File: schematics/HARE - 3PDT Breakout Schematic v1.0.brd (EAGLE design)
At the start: 30.5 x 20 mm, 4 parts, among them SW1 3PDTBLUE

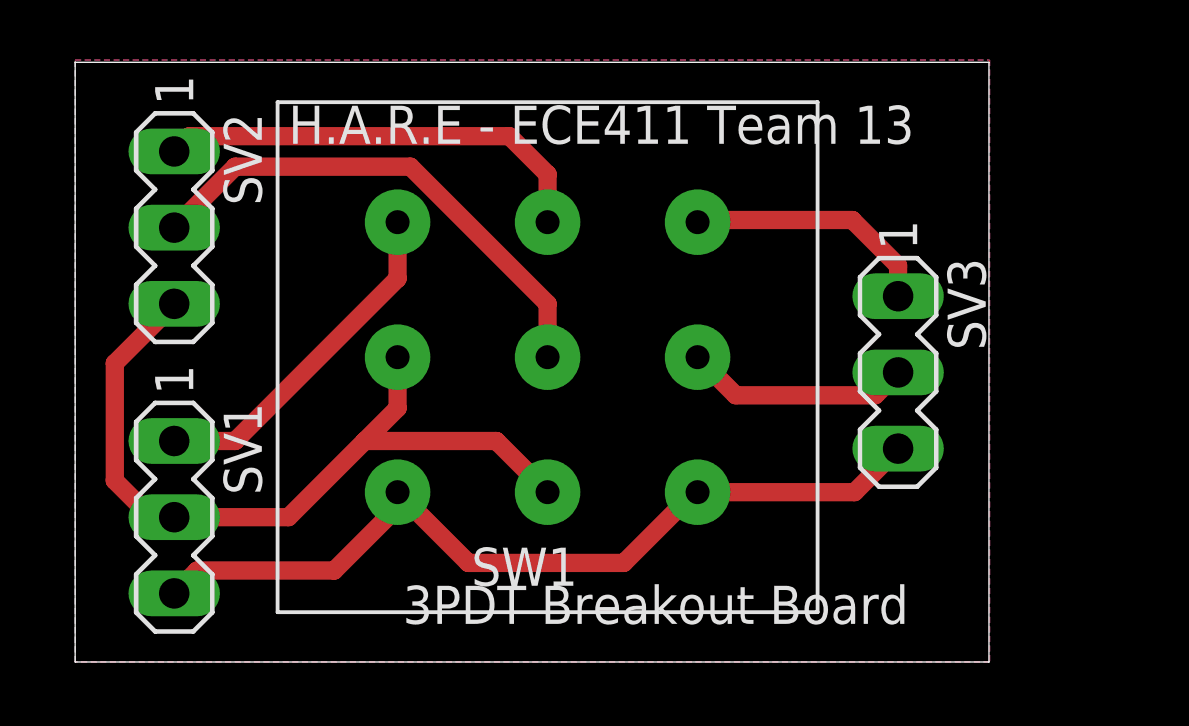
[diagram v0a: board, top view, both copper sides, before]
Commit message: adapting 3PDT breakout board to mate with HARE main board
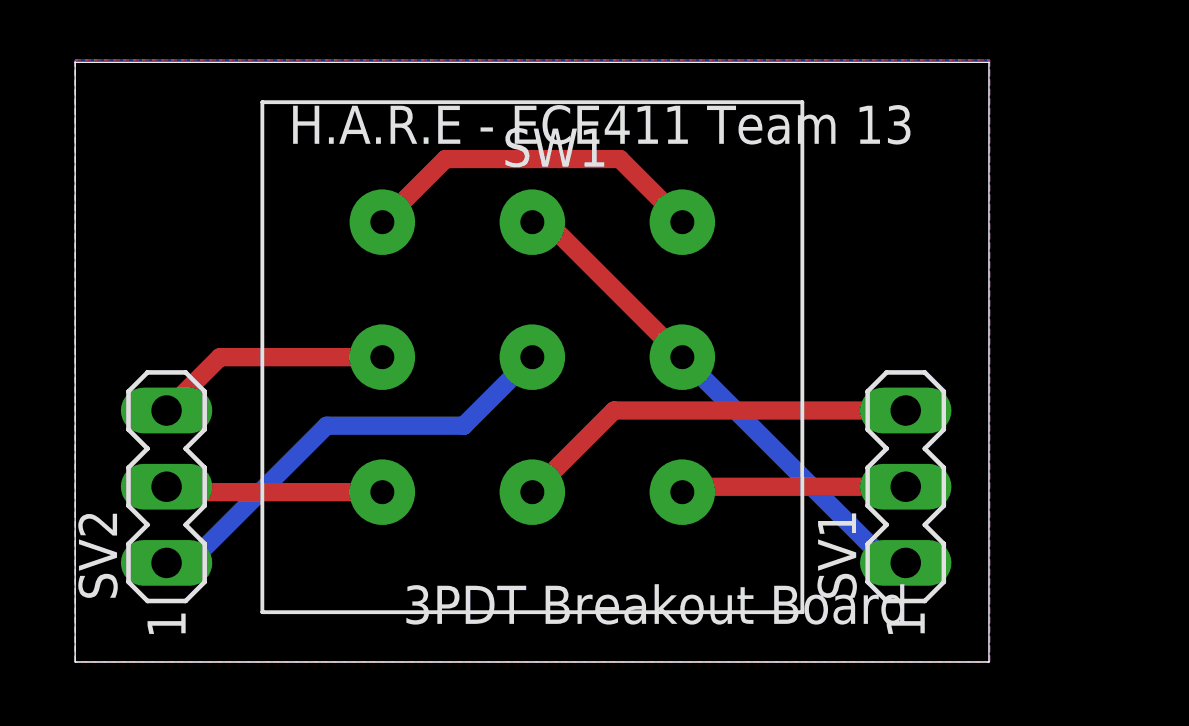
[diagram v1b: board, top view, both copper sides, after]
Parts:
- removed SV3: (no value), con-lstb:MA03-1
- moved SV1 24.4 mm to (27.7, 5.84), turned to 90 degrees
- moved SV2 8.64 mm to (3.05, 5.84), turned to 90 degrees
- moved SW1 0.51 mm to (15.2, 10.2), turned to 180 degrees
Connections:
- net ANALOG_IN: now also SV1.2; no longer SV1.1
- net ANALOG_OUT: now also SV2.3; no longer SV3.2
- net BYPASS: no longer SV1.3, SV3.3
- net GND: now also SV2.1; no longer SV2.2
- net INPUT: now also SV1.1; no longer SV1.2, SV2.3
- net OUTPUT: now also SV2.2; no longer SV3.1
- net PWR_LED: now also SV1.3; no longer SV2.1
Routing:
- net BYPASS: track 28.4 -> 11.8 mm
- net INPUT: track 26.7 -> 17.2 mm
- net ANALOG_IN: track 11.6 -> 7.52 mm
- net GND: track 17.0 -> 15.0 mm
- net PWR_LED: track 14.8 -> 13.6 mm
- net OUTPUT: track 8.36 -> 7.27 mm
- added copper zone on layer 16, net N$1
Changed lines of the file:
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@@
 <?xml version="1.0" encoding="utf-8"?>
 <!DOCTYPE eagle SYSTEM "eagle.dtd">
-<eagle version="8.4.0">
+<eagle version="8.4.1">
 <drawing>
 <settings>
@@
 <param name="dpMaxLengthDifference" value="10mm"/>
 <param name="dpGapFactor" value="2.5"/>
+<param name="checkAngle" value="0"/>
 <param name="checkFont" value="1"/>
 <param name="checkRestrict" value="1"/>
@@
 </autorouter>
 <elements>
-<element name="SW1" library="gm-switches" package="CHINABLUE" value="3PDTBLUE" x="15.748" y="10.16"/>
-<element name="SV1" library="con-lstb" package="MA03-1" value="" x="3.302" y="4.826" rot="R270">
-<attribute name="MF" value="" x="3.302" y="4.826" size="1.778" layer="27" rot="R270" display="off"/>
-<attribute name="MPN" value="" x="3.302" y="4.826" size="1.778" layer="27" rot="R270" display="off"/>
-<attribute name="OC_FARNELL" value="unknown" x="3.302" y="4.826" size="1.778" layer="27" rot="R270" display="off"/>
-<attribute name="OC_NEWARK" value="unknown" x="3.302" y="4.826" size="1.778" layer="27" rot="R270" display="off"/>
+<element name="SW1" library="gm-switches" package="CHINABLUE" value="3PDTBLUE" x="15.24" y="10.16" rot="R180"/>
+<element name="SV1" library="con-lstb" package="MA03-1" value="" x="27.686" y="5.842" rot="R90">
+<attribute name="MF" value="" x="27.686" y="5.842" size="1.778" layer="27" rot="R90" display="off"/>
+<attribute name="MPN" value="" x="27.686" y="5.842" size="1.778" layer="27" rot="R90" display="off"/>
+<attribute name="OC_FARNELL" value="unknown" x="27.686" y="5.842" size="1.778" layer="27" rot="R90" display="off"/>
+<attribute name="OC_NEWARK" value="unknown" x="27.686" y="5.842" size="1.778" layer="27" rot="R90" display="off"/>
 </element>
-<element name="SV2" library="con-lstb" package="MA03-1" value="" x="3.302" y="14.478" rot="R270">
-<attribute name="MF" value="" x="3.302" y="14.478" size="1.778" layer="27" rot="R270" display="off"/>
-<attribute name="MPN" value="" x="3.302" y="14.478" size="1.778" layer="27" rot="R270" display="off"/>
-<attribute name="OC_FARNELL" value="unknown" x="3.302" y="14.478" size="1.778" layer="27" rot="R270" display="off"/>
-<attribute name="OC_NEWARK" value="unknown" x="3.302" y="14.478" size="1.778" layer="27" rot="R270" display="off"/>
-</element>
-<element name="SV3" library="con-lstb" package="MA03-1" value="" x="27.432" y="9.652" rot="R270">
-<attribute name="MF" value="" x="27.432" y="9.652" size="1.778" layer="27" rot="R270" display="off"/>
-<attribute name="MPN" value="" x="27.432" y="9.652" size="1.778" layer="27" rot="R270" display="off"/>
-<attribute name="OC_FARNELL" value="unknown" x="27.432" y="9.652" size="1.778" layer="27" rot="R270" display="off"/>
-<attribute name="OC_NEWARK" value="unknown" x="27.432" y="9.652" size="1.778" layer="27" rot="R270" display="off"/>
+<element name="SV2" library="con-lstb" package="MA03-1" value="" x="3.048" y="5.842" rot="R90">
+<attribute name="MF" value="" x="3.048" y="5.842" size="1.778" layer="27" rot="R90" display="off"/>
+<attribute name="MPN" value="" x="3.048" y="5.842" size="1.778" layer="27" rot="R90" display="off"/>
+<attribute name="OC_FARNELL" value="unknown" x="3.048" y="5.842" size="1.778" layer="27" rot="R90" display="off"/>
+<attribute name="OC_NEWARK" value="unknown" x="3.048" y="5.842" size="1.778" layer="27" rot="R90" display="off"/>
 </element>
 </elements>
@@
 <contactref element="SW1" pad="A2"/>
 <contactref element="SW1" pad="B3"/>
-<contactref element="SV1" pad="2"/>
-<contactref element="SV2" pad="3"/>
-<wire x1="3.302" y1="11.938" x2="1.3208" y2="9.9568" width="0.6096" layer="1"/>
-<wire x1="1.3208" y1="6.0452" x2="2.54" y2="4.826" width="0.6096" layer="1"/>
-<wire x1="2.54" y1="4.826" x2="3.302" y2="4.826" width="0.6096" layer="1"/>
-<wire x1="1.3208" y1="9.9568" x2="1.3208" y2="6.0452" width="0.6096" layer="1"/>
-<wire x1="3.302" y1="4.826" x2="7.112" y2="4.826" width="0.6096" layer="1"/>
-<wire x1="9.652" y1="7.366" x2="14.042" y2="7.366" width="0.6096" layer="1"/>
-<wire x1="14.042" y1="7.366" x2="15.748" y2="5.66" width="0.6096" layer="1"/>
-<wire x1="7.112" y1="4.826" x2="9.652" y2="7.366" width="0.6096" layer="1"/>
-<wire x1="10.748" y1="10.16" x2="10.748" y2="8.462" width="0.6096" layer="1"/>
-<wire x1="10.748" y1="8.462" x2="9.652" y2="7.366" width="0.6096" layer="1"/>
+<wire x1="15.24" y1="14.66" x2="15.74" y2="14.66" width="0.6096" layer="1"/>
+<wire x1="15.74" y1="14.66" x2="20.24" y2="10.16" width="0.6096" layer="1"/>
+<contactref element="SV1" pad="1"/>
+<wire x1="20.24" y1="10.16" x2="27.098" y2="3.302" width="0.6096" layer="16"/>
+<wire x1="27.098" y1="3.302" x2="27.686" y2="3.302" width="0.6096" layer="16"/>
 </signal>
 <signal name="ANALOG_IN">
 <contactref element="SW1" pad="A1"/>
-<contactref element="SV1" pad="1"/>
-<wire x1="3.302" y1="7.366" x2="5.334" y2="7.366" width="0.6096" layer="1"/>
-<wire x1="10.748" y1="12.78" x2="10.748" y2="14.66" width="0.6096" layer="1"/>
-<wire x1="5.334" y1="7.366" x2="10.748" y2="12.78" width="0.6096" layer="1"/>
+<contactref element="SV1" pad="2"/>
+<wire x1="27.686" y1="5.842" x2="20.422" y2="5.842" width="0.6096" layer="1"/>
+<wire x1="20.422" y1="5.842" x2="20.24" y2="5.66" width="0.6096" layer="1"/>
 </signal>
 <signal name="BYPASS">
 <contactref element="SW1" pad="A3"/>
 <contactref element="SW1" pad="C3"/>
-<contactref element="SV1" pad="3"/>
-<contactref element="SV3" pad="3"/>
-<wire x1="3.302" y1="2.286" x2="4.064" y2="3.048" width="0.6096" layer="1"/>
-<wire x1="4.064" y1="3.048" x2="8.636" y2="3.048" width="0.6096" layer="1"/>
-<wire x1="8.636" y1="3.048" x2="10.748" y2="5.16" width="0.6096" layer="1"/>
-<wire x1="10.748" y1="5.16" x2="10.748" y2="5.66" width="0.6096" layer="1"/>
-<wire x1="10.748" y1="5.66" x2="13.106" y2="3.302" width="0.6096" layer="1"/>
-<wire x1="13.106" y1="3.302" x2="18.288" y2="3.302" width="0.6096" layer="1"/>
-<wire x1="18.288" y1="3.302" x2="20.646" y2="5.66" width="0.6096" layer="1"/>
-<wire x1="20.646" y1="5.66" x2="20.748" y2="5.66" width="0.6096" layer="1"/>
-<wire x1="20.748" y1="5.66" x2="25.98" y2="5.66" width="0.6096" layer="1"/>
-<wire x1="25.98" y1="5.66" x2="27.432" y2="7.112" width="0.6096" layer="1"/>
+<wire x1="10.24" y1="14.66" x2="12.344" y2="16.764" width="0.6096" layer="1"/>
+<wire x1="12.344" y1="16.764" x2="18.161" y2="16.764" width="0.6096" layer="1"/>
+<wire x1="18.161" y1="16.764" x2="19.859" y2="15.066" width="0.6096" layer="1"/>
+<wire x1="19.859" y1="15.066" x2="20.24" y2="14.66" width="0.6096" layer="1"/>
 </signal>
 <signal name="ANALOG_OUT">
 <contactref element="SW1" pad="C2"/>
-<contactref element="SV3" pad="2"/>
-<wire x1="20.748" y1="10.16" x2="22.018" y2="8.89" width="0.6096" layer="1"/>
-<wire x1="26.67" y1="8.89" x2="27.432" y2="9.652" width="0.6096" layer="1"/>
-<wire x1="22.018" y1="8.89" x2="26.67" y2="8.89" width="0.6096" layer="1"/>
+<contactref element="SV2" pad="3"/>
+<wire x1="10.24" y1="10.16" x2="4.826" y2="10.16" width="0.6096" layer="1"/>
+<wire x1="4.826" y1="10.16" x2="3.048" y2="8.382" width="0.6096" layer="1"/>
 </signal>
 <signal name="PWR_LED">
 <contactref element="SW1" pad="B1"/>
-<contactref element="SV2" pad="1"/>
-<wire x1="15.748" y1="14.66" x2="15.748" y2="16.256" width="0.6096" layer="1"/>
-<wire x1="15.748" y1="16.256" x2="14.478" y2="17.526" width="0.6096" layer="1"/>
-<wire x1="14.478" y1="17.526" x2="3.81" y2="17.526" width="0.6096" layer="1"/>
-<wire x1="3.81" y1="17.526" x2="3.302" y2="17.018" width="0.6096" layer="1"/>
+<contactref element="SV1" pad="3"/>
+<wire x1="15.24" y1="5.66" x2="17.962" y2="8.382" width="0.6096" layer="1"/>
+<wire x1="17.962" y1="8.382" x2="27.686" y2="8.382" width="0.6096" layer="1"/>
 </signal>
 <signal name="OUTPUT">
 <contactref element="SW1" pad="C1"/>
-<contactref element="SV3" pad="1"/>
-<wire x1="27.432" y1="12.192" x2="27.432" y2="13.208" width="0.6096" layer="1"/>
-<wire x1="27.432" y1="13.208" x2="25.908" y2="14.732" width="0.6096" layer="1"/>
-<wire x1="25.908" y1="14.732" x2="20.82" y2="14.732" width="0.6096" layer="1"/>
-<wire x1="20.82" y1="14.732" x2="20.748" y2="14.66" width="0.6096" layer="1"/>
+<contactref element="SV2" pad="2"/>
+<wire x1="10.24" y1="5.66" x2="3.23" y2="5.66" width="0.6096" layer="1"/>
+<wire x1="3.23" y1="5.66" x2="3.048" y2="5.842" width="0.6096" layer="1"/>
 </signal>
 <signal name="GND">
 <contactref element="SW1" pad="B2"/>
-<contactref element="SV2" pad="2"/>
 <polygon width="0.1524" layer="16">
 <vertex x="0" y="0"/>
@@
 <vertex x="30.48" y="0"/>
 </polygon>
-<wire x1="15.748" y1="10.16" x2="15.748" y2="11.938" width="0.6096" layer="1"/>
-<wire x1="15.748" y1="11.938" x2="11.176" y2="16.51" width="0.6096" layer="1"/>
-<wire x1="11.176" y1="16.51" x2="5.334" y2="16.51" width="0.6096" layer="1"/>
-<wire x1="5.334" y1="16.51" x2="3.302" y2="14.478" width="0.6096" layer="1"/>
+<contactref element="SV2" pad="1"/>
+<wire x1="15.24" y1="10.16" x2="12.954" y2="7.874" width="0.6096" layer="16"/>
+<wire x1="12.954" y1="7.874" x2="8.382" y2="7.874" width="0.6096" layer="16"/>
+<wire x1="8.382" y1="7.874" x2="3.81" y2="3.302" width="0.6096" layer="16"/>
+<wire x1="3.81" y1="3.302" x2="3.048" y2="3.302" width="0.6096" layer="16"/>
+</signal>
+<signal name="N$1">
+<polygon width="0.6096" layer="16">
+<vertex x="0" y="20.066"/>
+<vertex x="0" y="0"/>
+<vertex x="30.48" y="0"/>
+<vertex x="30.48" y="20.066"/>
+</polygon>
 </signal>
 </signals>

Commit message: Correctly placed the 3PDT switch connectors to mate with the main board
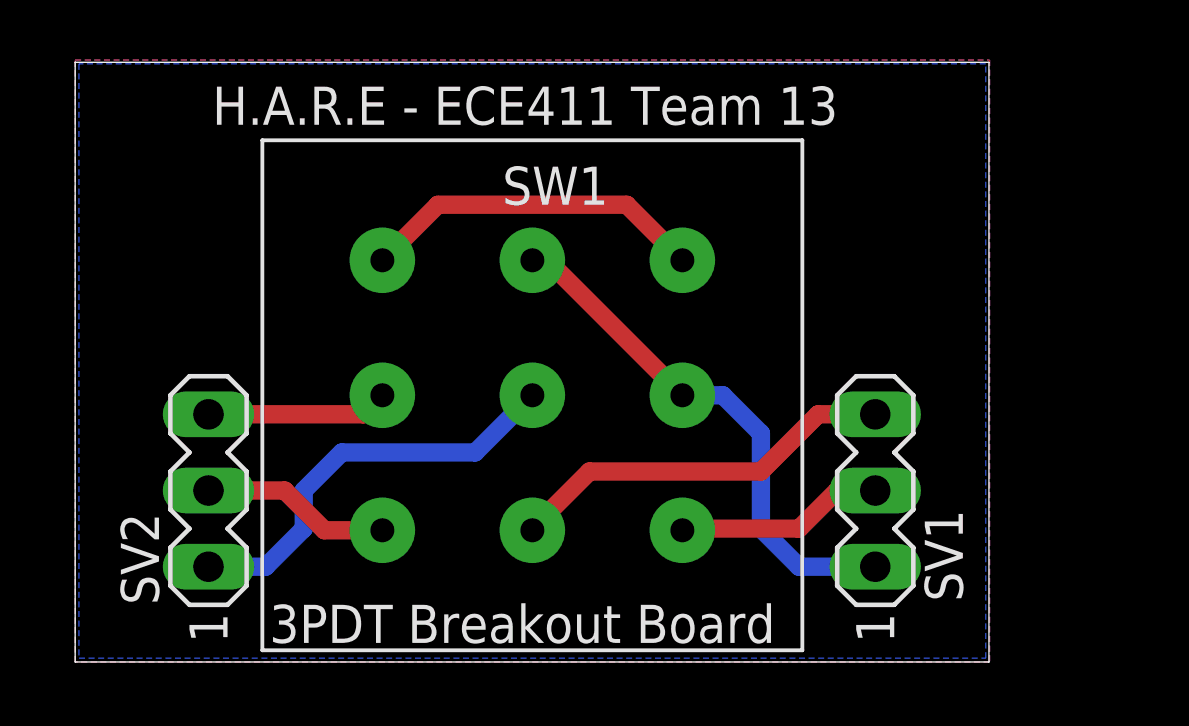
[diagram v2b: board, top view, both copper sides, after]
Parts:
- SV1: value (none) -> FtSW1
- SV2: value (none) -> FtSW2
- moved SV2 1.40 mm to (4.45, 5.71)
- moved SW1 1.27 mm to (15.2, 8.89)
- moved SV1 1.02 mm to (26.7, 5.71)
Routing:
- net ANALOG_OUT: track 7.93 -> 6.06 mm
- net GND: track 15.0 -> 13.9 mm
- net OUTPUT: track 7.27 -> 6.34 mm
- net ANALOG_IN: track 7.52 -> 6.98 mm
- net PWR_LED: track 13.6 -> 13.1 mm

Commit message: Shrank the size of the daughter board for the footswitch
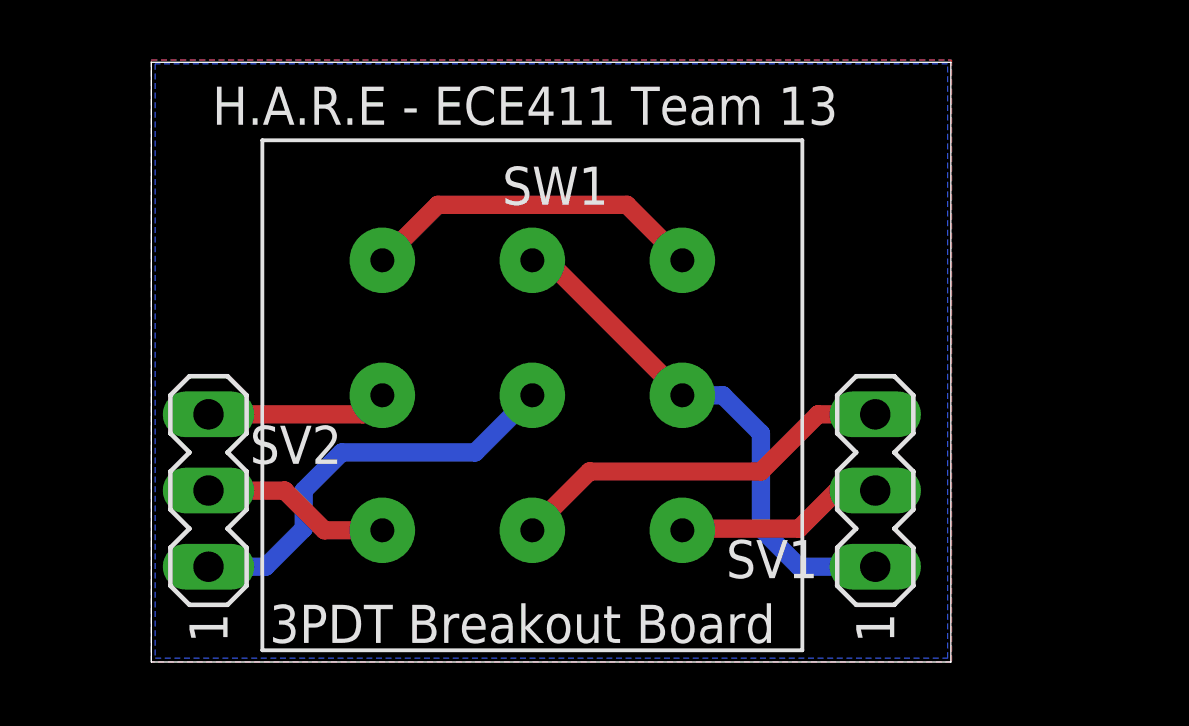
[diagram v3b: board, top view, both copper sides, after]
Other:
- board size 30.5 x 20 mm -> 26.7 x 20 mm
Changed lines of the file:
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@@
 <board>
 <plain>
-<wire x1="0" y1="0" x2="30.46" y2="0" width="0" layer="20"/>
-<wire x1="30.46" y1="0" x2="30.46" y2="19.99" width="0" layer="20"/>
-<wire x1="30.46" y1="19.99" x2="0" y2="19.99" width="0" layer="20"/>
-<wire x1="0" y1="19.99" x2="0" y2="0" width="0" layer="20"/>
+<wire x1="2.54" y1="0" x2="29.19" y2="0" width="0" layer="20"/>
+<wire x1="29.19" y1="0" x2="29.19" y2="19.99" width="0" layer="20"/>
+<wire x1="29.19" y1="19.99" x2="2.54" y2="19.99" width="0" layer="20"/>
+<wire x1="2.54" y1="19.99" x2="2.54" y2="0" width="0" layer="20"/>
 <text x="4.572" y="17.907" size="1.27" layer="25">H.A.R.E - ECE411 Team 13</text>
 <text x="6.477" y="0.635" size="1.27" layer="25">3PDT Breakout Board</text>
@@
 <attribute name="MF" value="" x="26.67" y="5.715" size="1.778" layer="27" rot="R90" display="off"/>
 <attribute name="MPN" value="" x="26.67" y="5.715" size="1.778" layer="27" rot="R90" display="off"/>
-<attribute name="NAME" x="28.321" y="5.08" size="1.27" layer="25" ratio="10" rot="R270"/>
+<attribute name="NAME" x="24.765" y="4.064" size="1.27" layer="25" ratio="10" rot="R180"/>
 <attribute name="OC_FARNELL" value="unknown" x="26.67" y="5.715" size="1.778" layer="27" rot="R90" display="off"/>
 <attribute name="OC_NEWARK" value="unknown" x="26.67" y="5.715" size="1.778" layer="27" rot="R90" display="off"/>
-<attribute name="VALUE" x="29.845" y="11.176" size="1.27" layer="27" ratio="10" rot="R180"/>
+<attribute name="VALUE" x="28.575" y="11.176" size="1.27" layer="27" ratio="10" rot="R180"/>
 </element>
 <element name="SV2" library="con-lstb" package="MA03-1" value="FtSW2" x="4.445" y="5.715" smashed="yes" rot="R90">
 <attribute name="MF" value="" x="4.445" y="5.715" size="1.778" layer="27" rot="R90" display="off"/>
 <attribute name="MPN" value="" x="4.445" y="5.715" size="1.778" layer="27" rot="R90" display="off"/>
-<attribute name="NAME" x="2.794" y="1.905" size="1.27" layer="25" ratio="10" rot="R90"/>
+<attribute name="NAME" x="8.89" y="7.874" size="1.27" layer="25" ratio="10" rot="R180"/>
 <attribute name="OC_FARNELL" value="unknown" x="4.445" y="5.715" size="1.778" layer="27" rot="R90" display="off"/>
 <attribute name="OC_NEWARK" value="unknown" x="4.445" y="5.715" size="1.778" layer="27" rot="R90" display="off"/>
@@
 <contactref element="SW1" pad="B2"/>
 <polygon width="0.1524" layer="16">
-<vertex x="0" y="0"/>
-<vertex x="0" y="20.066"/>
-<vertex x="30.48" y="20.066"/>
-<vertex x="30.48" y="0"/>
+<vertex x="2.54" y="0"/>
+<vertex x="2.54" y="20.066"/>
+<vertex x="29.21" y="20.066"/>
+<vertex x="29.21" y="0"/>
 </polygon>
 <polygon width="0.1524" layer="1">
-<vertex x="0" y="0"/>
-<vertex x="0" y="20.066"/>
-<vertex x="30.48" y="20.066"/>
-<vertex x="30.48" y="0"/>
+<vertex x="2.54" y="0"/>
+<vertex x="2.54" y="20.066"/>
+<vertex x="29.21" y="20.066"/>
+<vertex x="29.21" y="0"/>
 </polygon>
 <contactref element="SV2" pad="1"/>
@@
 <signal name="N$1">
 <polygon width="0.1524" layer="16" rank="2">
-<vertex x="0.127" y="19.939"/>
-<vertex x="0.127" y="0.127"/>
-<vertex x="30.353" y="0.127"/>
-<vertex x="30.353" y="19.939"/>
+<vertex x="2.667" y="19.939"/>
+<vertex x="2.667" y="0.127"/>
+<vertex x="29.083" y="0.127"/>
+<vertex x="29.083" y="19.939"/>
 </polygon>
 </signal>
